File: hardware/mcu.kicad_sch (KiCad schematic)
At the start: 21 parts, among them J201 STDC14

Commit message: work on layout
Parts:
- J201: footprint Connector_PinSocket_1.27mm:PinSocket_2x07_P1.27mm_Vertical -> Connector_PinHeader_1.27mm:PinHeader_2x07_P1.27mm_Vertical
- U?: value STM32G431CBUx -> STM32G431
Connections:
- net ~{SPI3_CSn}: now also U?.24 (PB11); no longer U?.29 (PC6)
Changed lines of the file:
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@@
+    (stroke (width 0) (type default))
+  )
+  (wire (pts (xy 64.77 115.57) (xy 69.85 115.57))
     (stroke (width 0) (type default))
   )
@@
     (effects (font (size 1.27 1.27)) (justify right))
   )
-  (hierarchical_label "~{SPI3_CSn}" (shape output) (at 64.77 69.85 180) (fields_autoplaced)
+  (hierarchical_label "~{SPI3_CSn}" (shape output) (at 64.77 115.57 180) (fields_autoplaced)
     (effects (font (size 1.27 1.27)) (justify right))
   )
@@
       (effects (font (size 1.27 1.27)) (justify left))
     )
-    (property "Value" "STM32G431CBUx" (at 89.5859 135.89 0)
+    (property "Value" "STM32G431" (at 89.5859 135.89 0)
       (effects (font (size 1.27 1.27)) (justify left))
     )
@@
         )
         (path "/bcb2c98d-7159-437a-9ffb-b81c5fcc4307/ed84ebbf-b2e5-4959-b495-bf58cd9b4c8c"
-          (reference "R?") (unit 1)
+          (reference "R206") (unit 1)
         )
       )
@@
         )
         (path "/bcb2c98d-7159-437a-9ffb-b81c5fcc4307/ed84ebbf-b2e5-4959-b495-bf58cd9b4c8c"
-          (reference "R?") (unit 1)
+          (reference "R207") (unit 1)
         )
       )
@@
       (effects (font (size 1.27 1.27)) (justify right))
     )
-    (property "Footprint" "Connector_PinSocket_1.27mm:PinSocket_2x07_P1.27mm_Vertical" (at 189.23 109.22 0)
-      (effects (font (size 1.27 1.27)) hide)
-    )
+    (property "Footprint" "Connector_PinHeader_1.27mm:PinHeader_2x07_P1.27mm_Vertical" (at 189.23 109.22 0)
+      (effects (font (size 1.27 1.27)) hide)
+    )

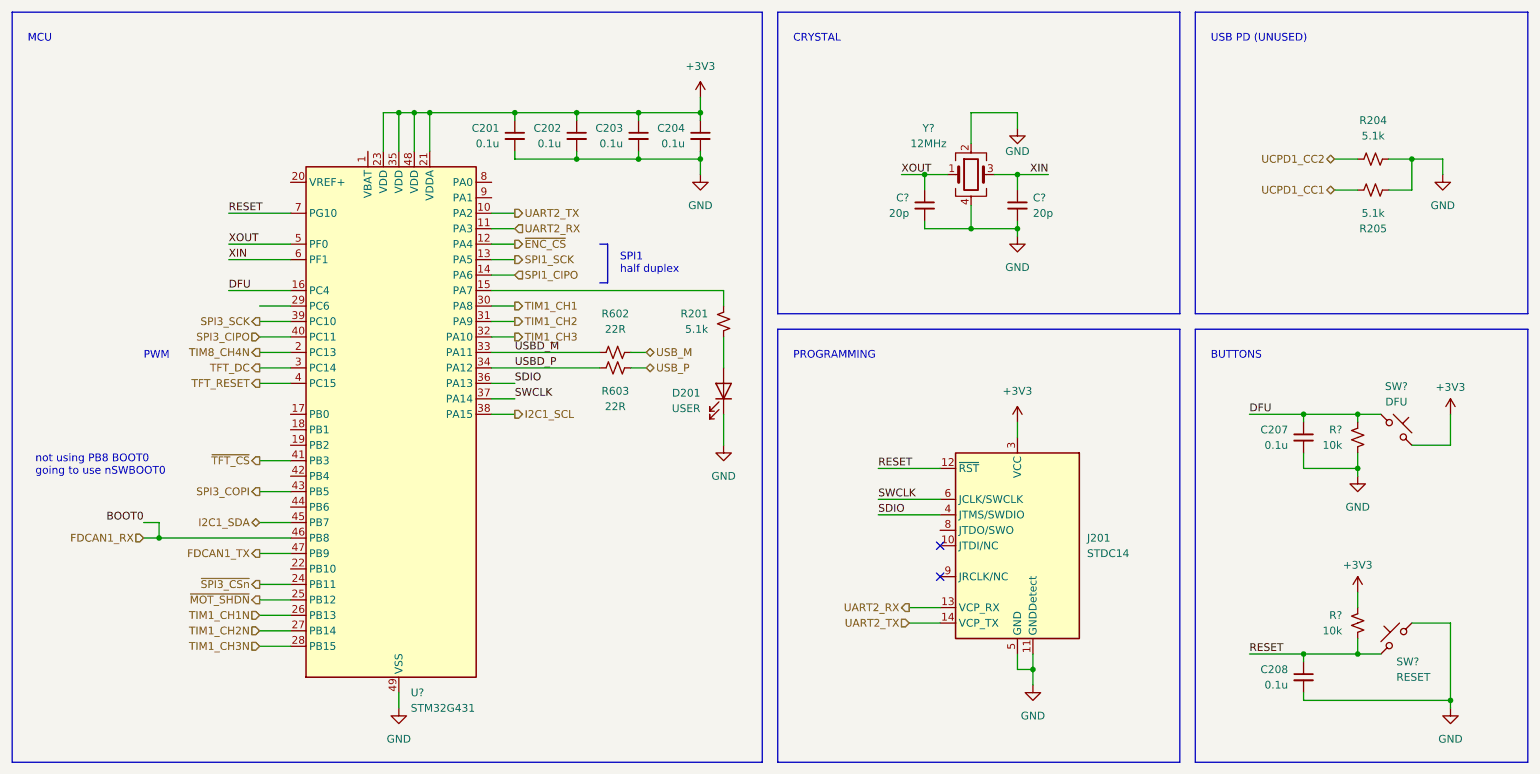
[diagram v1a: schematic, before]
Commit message: update schematic (Vref+ tie to Vdd) and go through ERC check
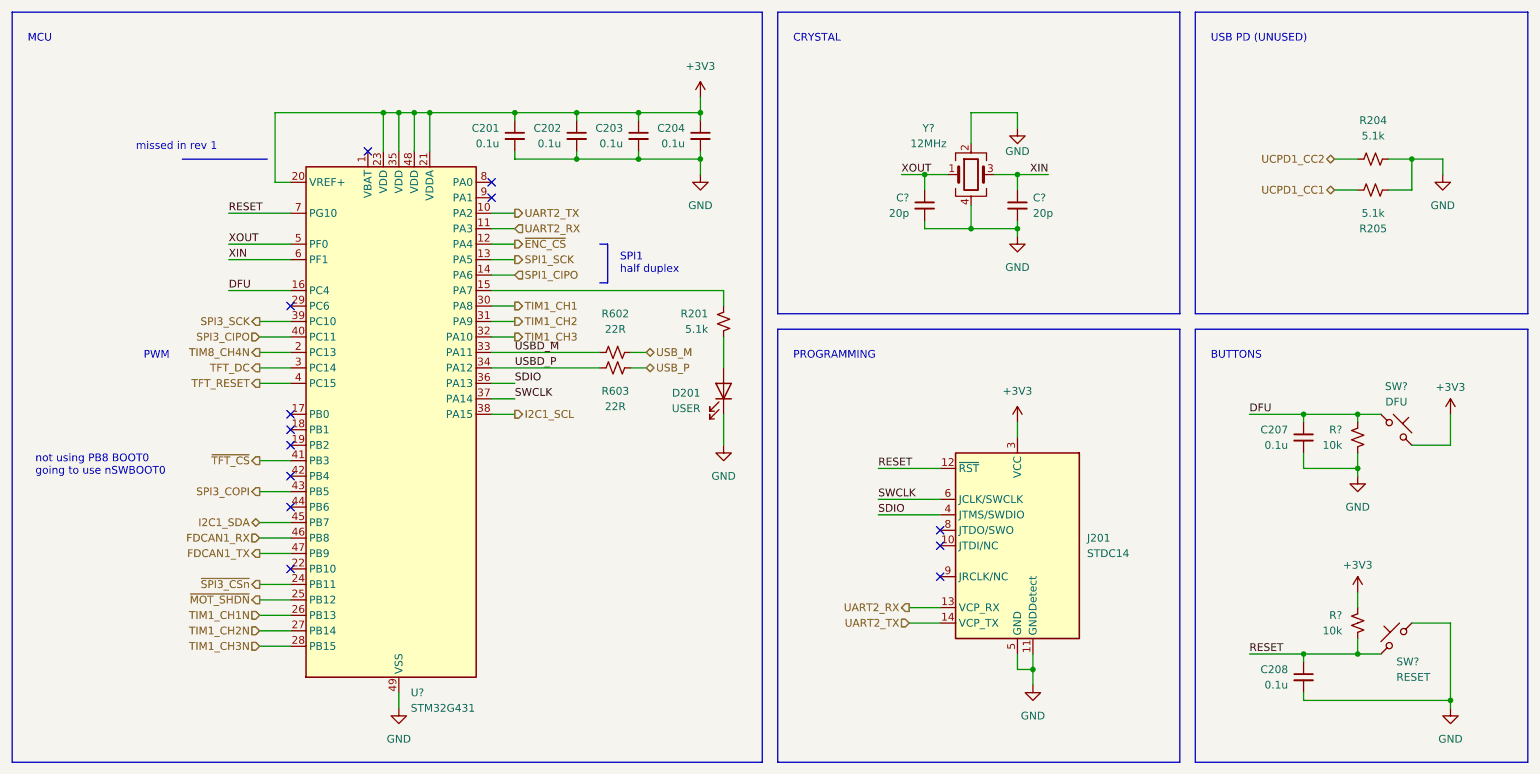
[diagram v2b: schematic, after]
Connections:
- net +3V3: now also U?.20 (VREF+)
- no-connect marks 2 -> 13
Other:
- note added: "missed in rev 1"
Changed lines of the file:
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@@
   (junction (at 92.71 38.1) (diameter 0) (color 0 0 0 0)
   )
-  (junction (at 48.26 107.95) (diameter 0) (color 0 0 0 0)
-  )
   (junction (at 236.22 87.63) (diameter 0) (color 0 0 0 0)
   )
+  (junction (at 85.09 38.1) (diameter 0) (color 0 0 0 0)
+  )
   (junction (at 181.61 57.15) (diameter 0) (color 0 0 0 0)
   )
   (junction (at 245.11 96.52) (diameter 0) (color 0 0 0 0)
   )
+  (no_connect (at 69.85 102.87))
+  (no_connect (at 176.53 106.68))
+  (no_connect (at 69.85 92.71))
+  (no_connect (at 69.85 97.79))
   (no_connect (at 176.53 114.3))
+  (no_connect (at 102.87 49.53))
+  (no_connect (at 69.85 69.85))
+  (no_connect (at 82.55 44.45))
+  (no_connect (at 102.87 52.07))
+  (no_connect (at 69.85 87.63))
+  (no_connect (at 69.85 113.03))
   (no_connect (at 176.53 109.22))
+  (no_connect (at 69.85 90.17))
   (wire (pts (xy 227.33 87.63) (xy 236.22 87.63))
     (stroke (width 0) (type default))
@@
     (stroke (width 0) (type default))
   )
+  (wire (pts (xy 67.31 49.53) (xy 67.31 38.1))
+    (stroke (width 0) (type default))
+  )
   (wire (pts (xy 173.99 48.26) (xy 173.99 50.8))
     (stroke (width 0) (type default))
@@
     (stroke (width 0) (type default))
   )
-  (wire (pts (xy 48.26 105.41) (xy 48.26 107.95))
-    (stroke (width 0) (type default))
-  )
   (wire (pts (xy 116.84 38.1) (xy 116.84 39.37))
     (stroke (width 0) (type default))
@@
     (stroke (width 0) (type default))
   )
-  (wire (pts (xy 64.77 69.85) (xy 69.85 69.85))
-    (stroke (width 0) (type default))
-  )
   (wire (pts (xy 59.69 62.23) (xy 69.85 62.23))
     (stroke (width 0) (type default))
@@
     (stroke (width 0) (type default))
   )
+  (polyline (pts (xy 52.07 45.72) (xy 66.04 45.72))
+    (stroke (width 0) (type default))
+  )
   (polyline (pts (xy 120.65 66.04) (xy 121.92 66.04))
     (stroke (width 0) (type default))
   )
+  (wire (pts (xy 69.85 49.53) (xy 67.31 49.53))
+    (stroke (width 0) (type default))
+  )
   (wire (pts (xy 102.87 72.39) (xy 106.68 72.39))
     (stroke (width 0) (type default))
@@
     (stroke (width 0) (type default))
   )
-  (wire (pts (xy 48.26 107.95) (xy 69.85 107.95))
+  (wire (pts (xy 64.77 107.95) (xy 69.85 107.95))
     (stroke (width 0) (type default))
   )
@@
     (stroke (width 0) (type default))
   )
-  (wire (pts (xy 45.72 105.41) (xy 48.26 105.41))
-    (stroke (width 0) (type default))
-  )
   (wire (pts (xy 102.87 59.69) (xy 106.68 59.69))
     (stroke (width 0) (type default))
@@
     (stroke (width 0) (type default))
   )
+  (wire (pts (xy 67.31 38.1) (xy 85.09 38.1))
+    (stroke (width 0) (type default))
+  )
   (wire (pts (xy 64.77 120.65) (xy 69.85 120.65))
     (stroke (width 0) (type default))
   )
-  (wire (pts (xy 45.72 107.95) (xy 48.26 107.95))
-    (stroke (width 0) (type default))
-  )
   (wire (pts (xy 102.87 69.85) (xy 106.68 69.85))
     (stroke (width 0) (type default))
@@
   )
   (text "MCU" (at 26.67 26.67 0)
+    (effects (font (size 1.27 1.27)) (justify left bottom))
+  )
+  (text "missed in rev 1" (at 44.45 44.45 0)
     (effects (font (size 1.27 1.27)) (justify left bottom))
   )
@@
     (effects (font (size 1.27 1.27)) (justify left bottom))
   )
-  (label "BOOT0" (at 45.72 105.41 180) (fields_autoplaced)
-    (effects (font (size 1.27 1.27)) (justify right bottom))
-  )
   (label "SDIO" (at 106.68 82.55 0) (fields_autoplaced)
     (effects (font (size 1.27 1.27)) (justify left bottom))
@@
     (effects (font (size 1.27 1.27)) (justify left bottom))
   )
-  (hierarchical_label "FDCAN1_RX" (shape input) (at 45.72 107.95 180) (fields_autoplaced)
+  (hierarchical_label "FDCAN1_RX" (shape input) (at 64.77 107.95 180) (fields_autoplaced)
     (effects (font (size 1.27 1.27)) (justify right))
   )

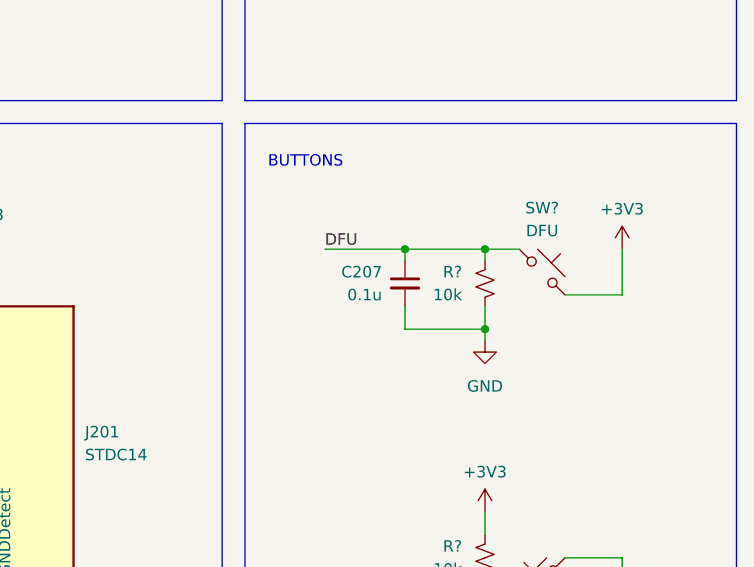
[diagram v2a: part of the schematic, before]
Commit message: update schematic to remove debounce cap
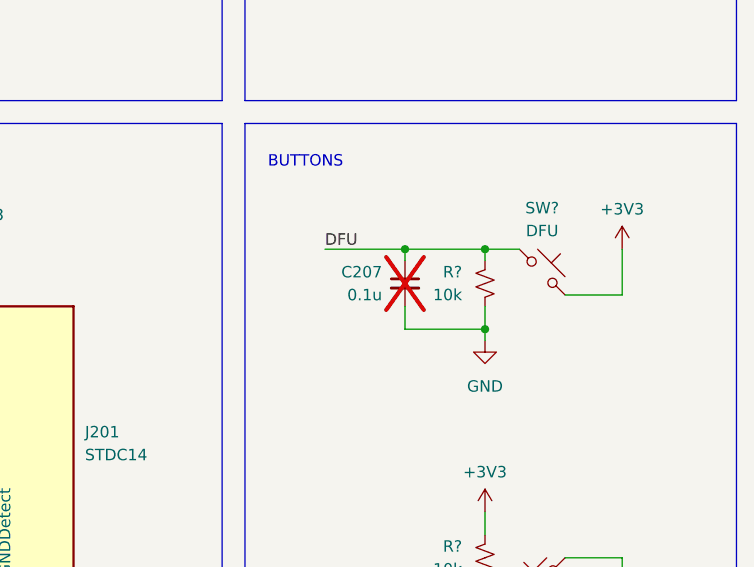
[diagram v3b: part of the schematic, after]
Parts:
- C207: now not fitted; now left out of the parts list
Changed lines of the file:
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@@
   )
   (symbol (lib_id "Device:C_Small") (at 236.22 91.44 0) (unit 1)
-    (in_bom yes) (on_board yes) (dnp no)
+    (in_bom no) (on_board yes) (dnp yes)
     (property "Reference" "C207" (at 233.68 90.1763 0)
       (effects (font (size 1.27 1.27)) (justify right))

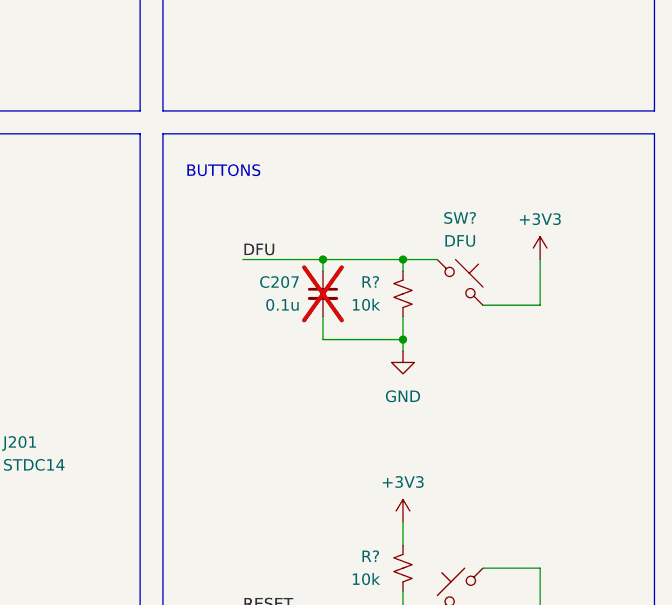
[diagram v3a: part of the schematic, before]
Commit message: get canbus working
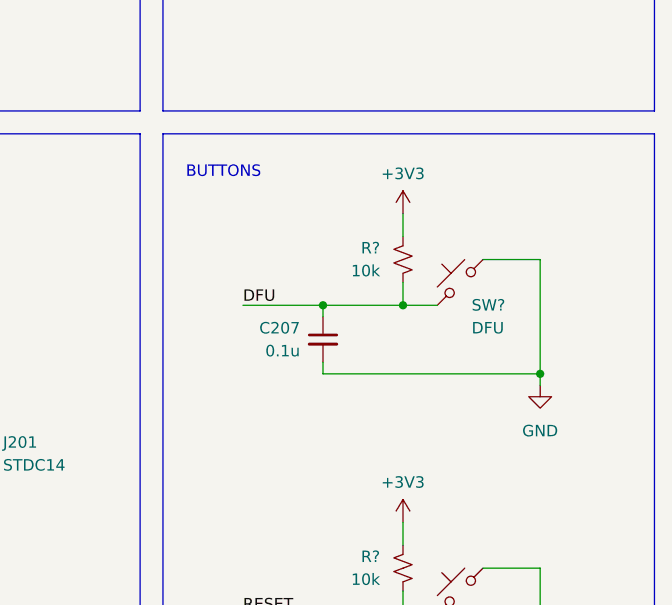
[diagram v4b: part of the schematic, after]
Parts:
- C207: now fitted; now in the parts list
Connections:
- net +3V3: now also R?.1; no longer SW?.2
- net DFU: now also R?.2; no longer R?.1
- net GND: now also SW?.2; no longer R?.2
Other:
- moved on the sheet: R?, SW?
